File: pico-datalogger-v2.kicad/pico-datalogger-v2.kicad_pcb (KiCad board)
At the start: 2 copper layers, 46 x 59.5 mm, 30 parts, among them J1 JST-PH2 Bat, J10 Conn_PCB_2, J11 Conn_I2C1, J12 Conn_UART, J2 Conn_Pico_Left, J3 Conn_Pico_Right, J4 Alt-Bat, J5 Conn_LoRa, J6 Conn_Display, J7 Conn_PCB_1, J8 Conn_ADC, J9 Conn_I2C0, Q1 AO3401A, U1 74LVC2G74, U2 PCF8523T, U4 XTSD, Y1 Crystal

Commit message: preliminary routing
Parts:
- added G***: LOGO, LOGO, B.Cu at (128.5, 124.7)
- J12: value Conn_UART -> Conn_UART_5V
- moved J5 8.84 mm to (94.1, 136.2)
- moved R4 5.37 mm to (103.4, 109.0), turned to 0 degrees
- moved J11 2.62 mm to (108.9, 125.1)
- moved R3 2.26 mm to (103.4, 107.7)
- moved J10 1.90 mm to (94.1, 124.7)
- moved J7 1.82 mm to (109.0, 154.8)
- moved R1 1.32 mm to (105.3, 115.5), turned to 90 degrees
- moved C2 1.03 mm to (105.3, 112.9)
- moved U2 1.03 mm to (108.1, 109.6)
- moved Y1 1.03 mm to (113.2, 110.8)
- moved C1 0.63 mm to (112.6, 114.9)
- moved U1 0.63 mm to (109.0, 116.0)
- moved R2 0.63 mm to (113.1, 116.5)
- moved J9 0.61 mm to (108.9, 101.1)
- moved JP1 0.41 mm to (121.5, 102.5)
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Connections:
- J10 pad 2: /PDM_DAT -> /SWD
- J10 pad 3: /SDA -> /PDM_DAT
- J10 pad 4: /SCL -> /SWA
- J10 pad 5: /SWD -> /SDA
- J10 pad 6: /SWA -> /SCL
- J12 pad 1: GND -> /RX
- J12 pad 2: +3V3 -> /TX
- J12 pad 3: /TX -> GND
- J12 pad 4: /RX -> /VBUS
- J2 pad 10: /Lora_RST -> /SWA
- J2 pad 12: /Lora_CS -> /SWB
- J2 pad 16: /SWA -> /Lora_RST
- J2 pad 17: /SWB -> /Lora_CS
- J3 pad 1: unconnected-(J3-Pad1) -> /VBUS
- J5 pad 1: /Lora_RST -> /MISO1
- J5 pad 2: /Lora_CS -> /SCLK1
- J5 pad 4: /MISO1 -> /Lora_RST
- J5 pad 5: /SCLK1 -> /Lora_CS
- J6 pad 3: /Display_BUSY -> /Display_RST
- J6 pad 4: /Display_RST -> /Display_BUSY
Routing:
- net +3V3: track 0.00 -> 107.3 mm, vias 0 -> 3
- net +BATT: track 0.00 -> 63.2 mm
- net /SDA: track 0.00 -> 48.0 mm
- net /SCL: track 0.00 -> 37.7 mm, vias 0 -> 1
- net /PDM_DAT: track 0.00 -> 29.6 mm
- net /VBUS: track 0.00 -> 28.3 mm
- net /MOSI0: track 0.00 -> 27.0 mm
- net /Display_BUSY: track 0.00 -> 26.3 mm
- net /RX: track 0.00 -> 25.0 mm, vias 0 -> 1
- net Net-(BT1-Pad1): track 0.00 -> 24.0 mm
- net /TX: track 0.00 -> 23.7 mm
- net /SWC: track 0.00 -> 21.8 mm, vias 0 -> 1
- net /~{ON}: track 0.00 -> 19.1 mm, vias 0 -> 2
- net /GP27_ADC1: track 0.00 -> 15.7 mm
- net /Display_RST: track 0.00 -> 15.0 mm
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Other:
- board text removed: "On"

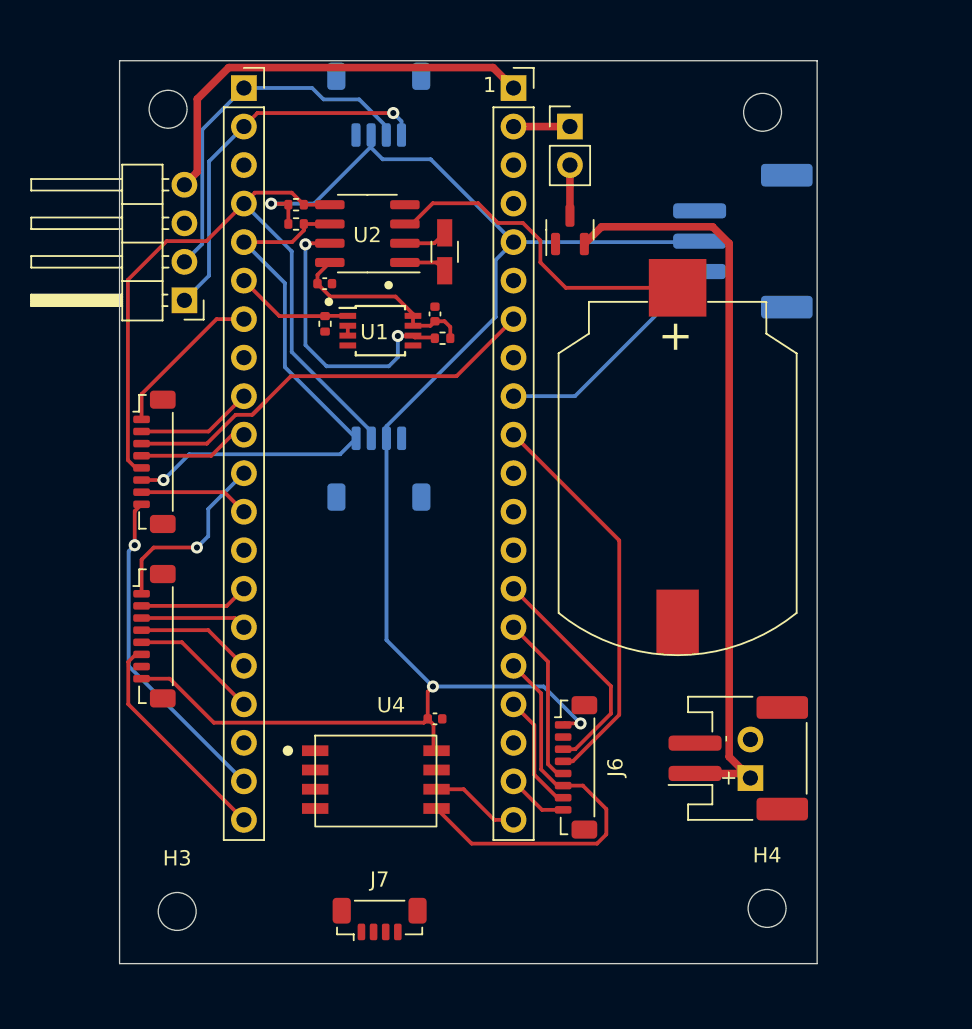
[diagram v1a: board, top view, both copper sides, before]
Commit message: further routing and layout work
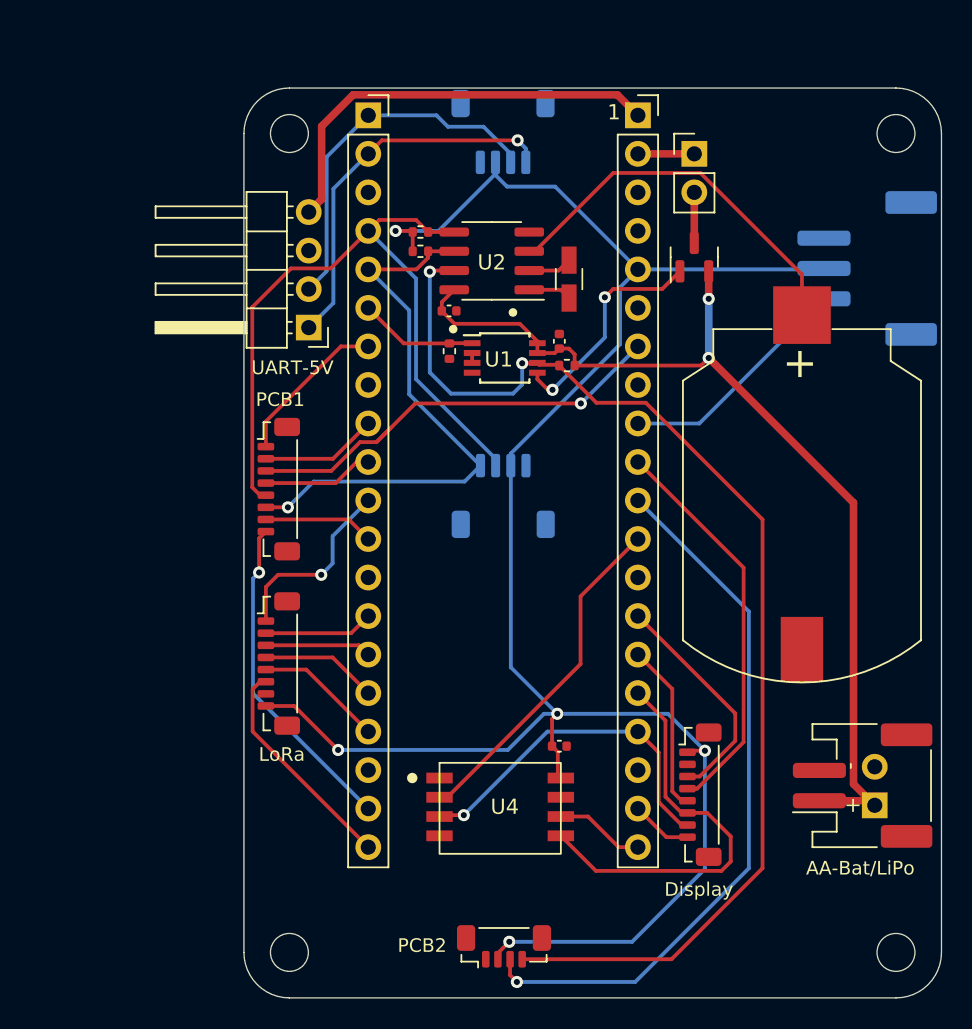
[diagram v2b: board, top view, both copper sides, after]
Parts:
- moved H4 8.98 mm to (143.0, 157.0)
- moved H2 8.91 mm to (143.0, 103.0)
- moved J1 8.40 mm to (140.8, 146.0)
- moved BT1 8.40 mm to (136.8, 126.0)
- moved C3 8.40 mm to (120.8, 143.4)
- moved J9 8.40 mm to (117.1, 102.9)
- moved R3 8.40 mm to (111.6, 109.5)
- moved U2 8.40 mm to (116.3, 111.4)
- moved U4 8.40 mm to (112.9, 145.5)
- moved C1 8.40 mm to (120.8, 116.7)
- moved C2 8.40 mm to (113.5, 114.7)
- moved J10 8.40 mm to (102.3, 126.5)
- moved J12 8.40 mm to (104.3, 115.8)
- moved J2 8.40 mm to (108.2, 101.8)
- moved J3 8.40 mm to (126.0, 101.8)
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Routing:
- net /~{ON}: track 19.1 -> 78.1 mm
- net /RUN: track 0.00 -> 47.4 mm, vias 0 -> 1
- net +3V3: track 107.3 -> 132.7 mm, vias 3 -> 5
- net /SD_CS: track 0.00 -> 22.7 mm
- net /SCLK0: track 7.74 -> 23.1 mm, vias 0 -> 1
- net /PC_GATE: track 0.00 -> 14.9 mm, vias 0 -> 2
- net Net-(BT1-Pad1): track 24.0 -> 27.9 mm
- net +BATT: track 63.2 -> 65.7 mm, vias 0 -> 2
- net /PDM_DAT: vias 0 -> 1
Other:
- board size 46 x 59.5 mm -> 46 x 60 mm
- board text added: "AA-Bat/LiPo"
- board text added: "ADC/1-Wire"
- board text added: "Display"
- board text added: "I2C0/UART-3V3"
- board text added: "I2C1"
- board text added: "LoRa"
- board text added: "PCB1"
- board text added: "PCB2"
- board text added: "UART-5V"

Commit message: added some more optional components (buttons, I2C-connector)
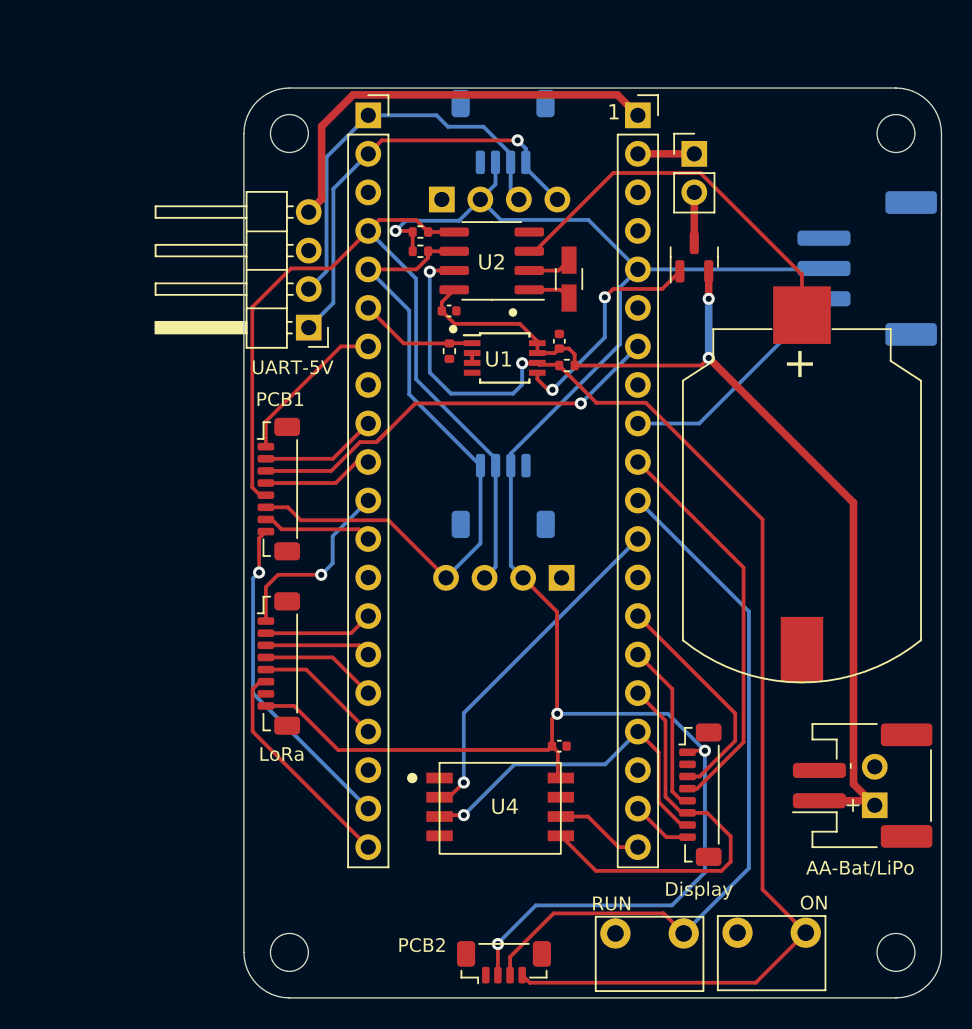
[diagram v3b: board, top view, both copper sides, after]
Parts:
- added J13: Conn_I2C1, Connector_PinHeader_2.54mm:PinHeader_1x04_P2.54mm_Vertical, B.Cu at (121.0, 132.3)
- added J14: Conn_I2C0, Connector_PinHeader_2.54mm:PinHeader_1x04_P2.54mm_Vertical, B.Cu at (113.0, 107.3)
- added SW1: SW_ON, user:SW_PUSH_1x_6mm, F.Cu at (132.6, 155.7)
- added SW2: SW_RUN, user:SW_PUSH_1x_6mm, F.Cu at (124.5, 155.8)
- moved J7 1.05 mm to (117.2, 157.7)
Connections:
- J3 pad 4: /3V3_EN -> unconnected-(J3-Pad4)
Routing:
- net /SDA: track 48.0 -> 55.7 mm
- net /~{ON}: track 78.1 -> 85.4 mm
- net /SCL: track 37.7 -> 44.6 mm, vias 1 -> 0
- net /RX: track 25.0 -> 28.3 mm
- net /TX: track 23.7 -> 26.4 mm
- net +3V3: track 132.7 -> 133.5 mm, vias 5 -> 4
- net /RUN: track 47.4 -> 47.8 mm, vias 1 -> 0
- net /SD_CS: track 22.7 -> 22.8 mm, vias 0 -> 1
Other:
- board text added: "ON"
- board text added: "RUN"

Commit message: make UART-5V compatible to Pimoroni PMS5003-adapter
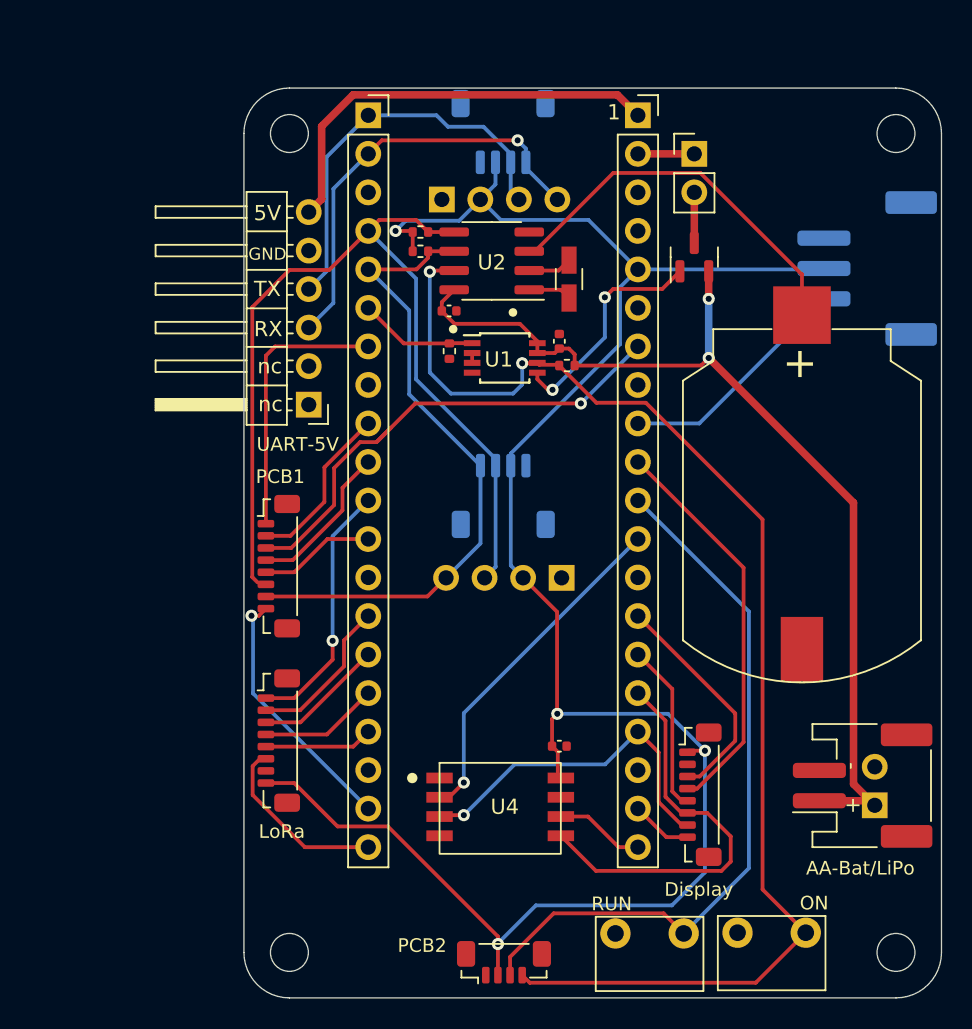
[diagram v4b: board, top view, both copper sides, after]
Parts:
- J12: footprint Connector_PinHeader_2.54mm:PinHeader_1x04_P2.54mm_Horizontal -> Connector_PinHeader_2.54mm:PinHeader_1x06_P2.54mm_Horizontal
- moved J5 5.08 mm to (102.3, 143.0)
- moved J10 5.08 mm to (102.3, 131.5)
- moved J12 5.08 mm to (104.3, 120.9)
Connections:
- J10 pad 5: /SDA -> /SWB
- J10 pad 6: /SCL -> /SDA
- J10 pad 7: /SWB -> /SCL
- J12 pad 1: /RX -> unconnected-(J12-Pad1)
- J12 pad 2: /TX -> unconnected-(J12-Pad2)
- J12 pad 3: GND -> /RX
- J12 pad 4: /VBUS -> /TX
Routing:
- net /PDM_CLK: track 10.5 -> 18.1 mm
- net /SDA: track 55.7 -> 61.0 mm
- net /SWC: track 21.8 -> 17.1 mm
- net /MISO1: track 12.4 -> 16.9 mm
- net /SWD: track 7.72 -> 11.2 mm
- net /PDM_DAT: track 29.6 -> 32.7 mm
- net /SCLK1: track 7.22 -> 10.3 mm
- net /SWA: track 7.33 -> 10.3 mm
- net /Lora_EN: track 14.7 -> 12.0 mm
- net /MOSI1: track 7.00 -> 8.60 mm
- net /SCL: track 44.6 -> 43.1 mm
- net /Lora_CS: track 8.44 -> 7.16 mm
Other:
- board text added: "3V3"
- board text added: "5V"
- board text added: "GND"
- board text added: "GP27"
- board text added: "RX"
- board text added: "TX"
- board text added: "nc"

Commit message: added copper-fills
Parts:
- moved C2 1.59 mm to (113.5, 116.3)
- moved R4 1.59 mm to (111.6, 112.4)
- moved Y1 1.59 mm to (121.4, 114.2)
- moved R3 1.59 mm to (111.6, 111.1)
- moved U2 1.59 mm to (116.3, 113.0)
- moved R1 1.30 mm to (113.5, 118.7)
- moved C1 1.30 mm to (120.8, 118.0)
- moved R2 1.30 mm to (121.3, 119.6)
- moved U1 1.30 mm to (117.2, 119.1)
- moved J14 0.95 mm to (113.0, 108.3)
- moved J9 0.20 mm to (117.1, 103.1)
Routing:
- net GND: track 0.00 -> 4.69 mm, vias 0 -> 17
- net /~{ON}: track 85.4 -> 81.6 mm
- net /PC_GATE: track 14.9 -> 16.2 mm
- net Net-(BT1-Pad1): track 27.9 -> 26.7 mm
- net /Display_BUSY: track 26.3 -> 27.5 mm
- net /RX: track 28.3 -> 29.4 mm
- net /Display_RST: track 15.0 -> 15.9 mm
- net +3V3: track 133.3 -> 134.1 mm
- net /TX: track 26.4 -> 27.1 mm
- net /GP4_DONE: track 7.73 -> 8.27 mm
- net /PDM_DAT: track 32.7 -> 32.2 mm
- added copper zone on B.Cu, net GND
- added copper zone on F.Cu, net GND
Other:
- board text added: "SCL"
- board text added: "SDA"
- board text added: "https://github.com/bablokb/pcb-pico-datalogger https://opendeved.net/ilce Rev 0.93"

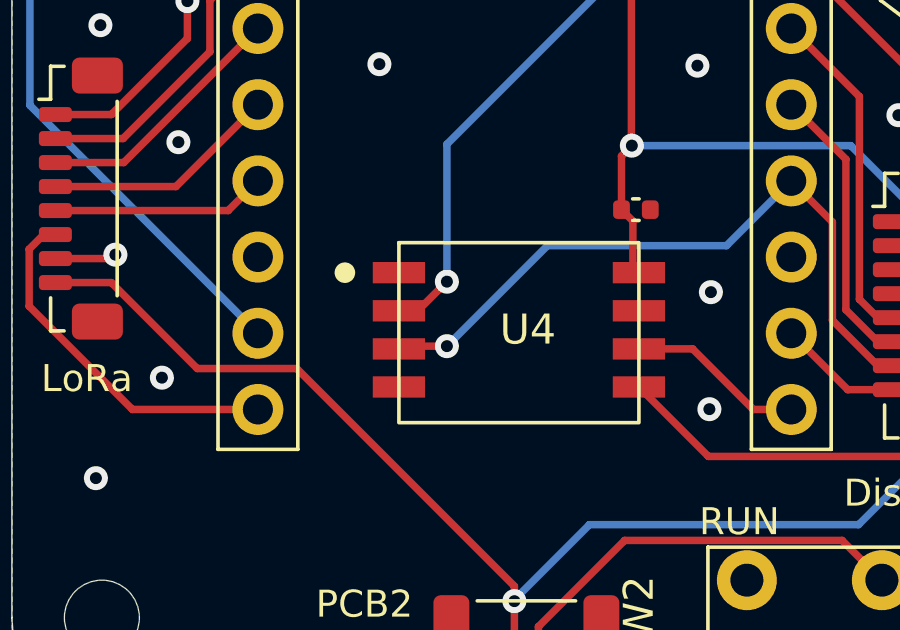
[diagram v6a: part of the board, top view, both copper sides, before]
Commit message: fixed rotation and part-placement
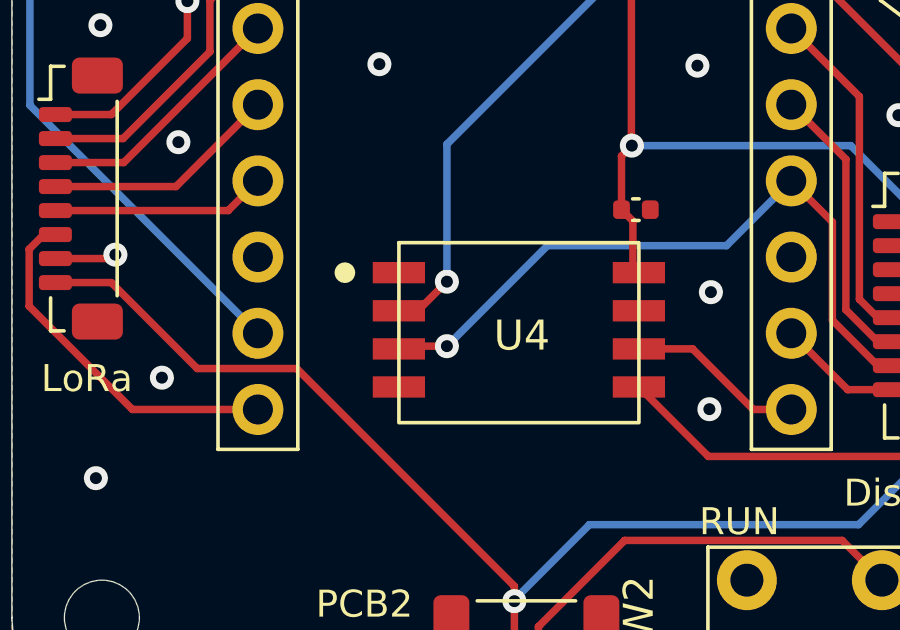
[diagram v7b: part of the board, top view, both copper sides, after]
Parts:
- moved U4 4.43 mm to (116.9, 147.4)
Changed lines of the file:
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@@
   )
   (footprint "user:LGA8_8X6" (layer "F.Cu")
-    (at 112.9 145.5)
+    (at 116.9 147.405)
     (property "LCSC" "C558837")
     (property "Sheetfile" "pico-datalogger-v2.kicad_sch")
     (property "Sheetname" "")
     (attr smd)
-    (fp_text reference "U4" (at 4.3 1.9 unlocked) (layer "F.SilkS")
+    (fp_text reference "U4" (at 0.1 0.195 unlocked) (layer "F.SilkS")
       (effects (font (size 1 1) (thickness 0.15)))
     )
-    (fp_text value "XTSD" (at 4 7 unlocked) (layer "F.Fab")
+    (fp_text value "XTSD" (at 0 5.095 unlocked) (layer "F.Fab")
       (effects (font (size 1 1) (thickness 0.15)))
     )
-    (fp_rect (start 0 -1) (end 8 5) (layer "F.SilkS") (width 0.12) (fill none))
-    (fp_circle (center -1.8 0) (end -1.517157 0) (layer "F.SilkS") (width 0.12) (fill solid))
-    (fp_rect (start -1.2 -1.4) (end 9.2 5.4) (layer "F.CrtYd") (width 0.12) (fill none))
-    (fp_rect (start -1.2 -1.4) (end 9.2 5.4) (layer "F.Fab") (width 0.1) (fill none))
-    (pad "1" smd rect (at 0 0) (size 1.741 0.711) (layers "F.Cu" "F.Paste" "F.Mask")
+    (fp_rect (start -4 -2.905) (end 4 3.095) (layer "F.SilkS") (width 0.12) (fill none))
+    (fp_circle (center -5.8 -1.905) (end -5.517157 -1.905) (layer "F.SilkS") (width 0.12) (fill solid))
+    (fp_rect (start -5.2 -3.305) (end 5.2 3.495) (layer "F.CrtYd") (width 0.12) (fill none))
+    (fp_rect (start -5.2 -3.305) (end 5.2 3.495) (layer "F.Fab") (width 0.1) (fill none))
+    (pad "1" smd rect (at -4 -1.905) (size 1.741 0.711) (layers "F.Cu" "F.Paste" "F.Mask")
       (net 42 "unconnected-(U4-Pad1)") (pinfunction "SD2/nc") (pintype "output+no_connect"))
-    (pad "2" smd rect (at 0 1.27) (size 1.741 0.711) (layers "F.Cu" "F.Paste" "F.Mask")
+    (pad "2" smd rect (at -4 -0.635) (size 1.741 0.711) (layers "F.Cu" "F.Paste" "F.Mask")
       (net 32 "/SD_CS") (pinfunction "SD3/CS") (pintype "input"))
-    (pad "3" smd rect (at 0 2.54) (size 1.741 0.711) (layers "F.Cu" "F.Paste" "F.Mask")
+    (pad "3" smd rect (at -4 0.635) (size 1.741 0.711) (layers "F.Cu" "F.Paste" "F.Mask")
       (net 36 "/SCLK0") (pinfunction "SCK/SCK") (pintype "input"))
-    (pad "4" smd rect (at 0 3.81) (size 1.741 0.711) (layers "F.Cu" "F.Paste" "F.Mask")
+    (pad "4" smd rect (at -4 1.905) (size 1.741 0.711) (layers "F.Cu" "F.Paste" "F.Mask")
       (net 2 "GND") (pinfunction "GND") (pintype "power_in"))
-    (pad "5" smd rect (at 8 3.81) (size 1.741 0.711) (layers "F.Cu" "F.Paste" "F.Mask")
+    (pad "5" smd rect (at 4 1.905) (size 1.741 0.711) (layers "F.Cu" "F.Paste" "F.Mask")
       (net 35 "/MOSI0") (pinfunction "CMD/MOSI") (pintype "input"))
-    (pad "6" smd rect (at 8 2.54) (size 1.741 0.711) (layers "F.Cu" "F.Paste" "F.Mask")
+    (pad "6" smd rect (at 4 0.635) (size 1.741 0.711) (layers "F.Cu" "F.Paste" "F.Mask")
       (net 38 "/MISO0") (pinfunction "SD0/MISO") (pintype "output"))
-    (pad "7" smd rect (at 8 1.27) (size 1.741 0.711) (layers "F.Cu" "F.Paste" "F.Mask")
+    (pad "7" smd rect (at 4 -0.635) (size 1.741 0.711) (layers "F.Cu" "F.Paste" "F.Mask")
       (net 43 "unconnected-(U4-Pad7)") (pinfunction "SD1/nc") (pintype "output+no_connect"))
-    (pad "8" smd rect (at 8 0) (size 1.741 0.711) (layers "F.Cu" "F.Paste" "F.Mask")
+    (pad "8" smd rect (at 4 -1.905) (size 1.741 0.711) (layers "F.Cu" "F.Paste" "F.Mask")
       (net 8 "+3V3") (pinfunction "VCC") (pintype "power_in"))
   )
